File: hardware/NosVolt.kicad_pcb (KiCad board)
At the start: 2 copper layers, 100 x 60 mm, 122 parts, among them CN201 100nF, J101 INPUTS, J102 OUTPUTS, J201 BAT_SENSE, J202 BAT_NTC, J401 USB_C_Receptacle_USB2.0_16P, Q1101 2N7002, Q1102 AO4407A, Q801 2N7002, Q802 AO4407A, Q901 2N7002, Q902 AO4407A, SW101 SW_Reset, SW102 SSSS811101, U1001 INA226, U101 GMT028-05, U102 ESP32-S3-WROOM-1, U1201 INA226, U201 ADS1115IDGS, U301 MP2307DN-LF-Z, U401 AP7361-33ER-13, U402 USBLC6-2SC6, U501 INA226, U601 INA226, U701 INA226

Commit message: reanotate
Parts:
- moved NT902 7.47 mm to (191.4, 82.0), turned to 90 degrees
- moved NT904 7.44 mm to (185.5, 86.5), turned to 180 degrees
- moved NT901 2.17 mm to (187.6, 79.0), turned to 90 degrees
- moved NT903 2.17 mm to (186.2, 80.7), turned to -90 degrees
- renumbered C601 to C301, C602 to C302, C701 to C401, C702 to C402, C1101 to C501, C1201 to C502, C1102 to C503, C1202 to C504, C901 to C601, C1001 to C602, C902 to C603, C1002 to C604, C801 to C701, C501 to C702, C802 to C703, C502 to C704, C401 to C801, C402 to C802, C403 to C803, C404 to C804, C405 to C805, C301 to C901, C302 to C902, C303 to C903, C304 to C904, C305 to C905, C306 to C906, C307 to C907, D401 to D801, F401 to F801, J401 to J801, L301 to L901, NT601 to NT301, NT602 to NT302, NT701 to NT401, NT702 to NT402, NT1101 to NT501, NT1201 to NT502, NT1202 to NT503, NT901 to NT601, NT1001 to NT602, NT1002 to NT603, NT801 to NT701, NT501 to NT702, NT502 to NT703, NT303 to NT901, NT304 to NT902, NT301 to NT903, NT302 to NT904, Q1101 to Q501, Q1102 to Q502, Q901 to Q601, Q902 to Q602, Q801 to Q701, Q802 to Q702, R601 to R301, R602 to R302, R603 to R303, R701 to R401, R702 to R402, R703 to R403, R1101 to R501, R1102 to R502, R1103 to R503, R1201 to R504, R1104 to R505, R1202 to R506, R1203 to R507, R901 to R601, R902 to R602, R903 to R603, R1001 to R604, R904 to R605, R1002 to R606, R1003 to R607, R801 to R701, R802 to R702, R803 to R703, R501 to R704, R804 to R705, R502 to R706, R503 to R707, R401 to R801, R402 to R802, R301 to R901, R302 to R902, R303 to R903, R304 to R904, U601 to U301, U701 to U401, U1201 to U501, U1001 to U601, U501 to U701, U401 to U801, U402 to U802, U301 to U901
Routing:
- net Net-(NT901-Pad2): track 0.00 -> 12.5 mm, vias 0 -> 2
- net /MP2307/SW: track 18.1 -> 5.59 mm, vias 2 -> 0
- net GND: track 74.4 -> 70.9 mm
- net Net-(NT904-Pad1): track 0.00 -> 3.56 mm

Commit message: text
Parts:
- moved C901 2.58 mm to (179.3, 76.8)
- moved C902 1.73 mm to (184.3, 76.8)
- moved NT901 0.72 mm to (188.0, 78.4), turned to 45 degrees
- moved R403 0.50 mm to (136.7, 57.8)
- moved L901 0.41 mm to (183.8, 84.0)
- moved NT904 0.38 mm to (185.1, 86.7)
- moved R904 0.31 mm to (189.6, 86.2)
- moved U101 0.28 mm to (152.7, 63.0)
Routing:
- net Net-(U901-BS): track 10.6 -> 8.28 mm
- net Net-(NT901-Pad2): track 12.5 -> 11.8 mm
- net Net-(NT904-Pad1): track 3.56 -> 4.15 mm
- net +3V3: vias 19 -> 18

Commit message: Add logo
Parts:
- added G***: LOGO, LOGO, F.Cu at (146.9, 82.6)
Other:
- board text added: "Version 1.0"

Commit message: page numbers
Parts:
- U901: footprint Package_SO:SOIC-8-1EP_3.9x4.9mm_P1.27mm_EP2.29x3mm_ThermalVias -> NosLib:SOIC-8-1EP_3.9x4.9mm_P1.27mm_EP2.29x3mm_ThermalVias
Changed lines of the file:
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@@
 		(embedded_fonts no)
 	)
-	(footprint "Package_SO:SOIC-8-1EP_3.9x4.9mm_P1.27mm_EP2.29x3mm_ThermalVias"
+	(footprint "NosLib:SOIC-8-1EP_3.9x4.9mm_P1.27mm_EP2.29x3mm_ThermalVias"
 		(layer "F.Cu")
 		(at 192.28 80.55)
@@
 			(pinfunction "GND")
 			(pintype "power_in")
-			(zone_connect 2)
 		)
 		(pad "5" smd roundrect
@@
 			(at -0.65 -1)
 			(size 0.5 0.5)
-			(drill 0.2)
+			(drill 0.3)
+			(property pad_prop_heatsink)
+			(layers "*.Cu" "B.Paste")
+			(remove_unused_layers no)
+			(net 69 "/MP2307/PWR_GND")
+			(pinfunction "EP")
+			(pintype "input")
+		)
+		(pad "9" thru_hole circle
+			(at -0.65 0)
+			(size 0.5 0.5)
+			(drill 0.3)
 			(property pad_prop_heatsink)
 			(layers "*.Cu")
@@
 		)
 		(pad "9" thru_hole circle
-			(at -0.65 0)
-			(size 0.5 0.5)
-			(drill 0.2)
-			(property pad_prop_heatsink)
-			(layers "*.Cu")
-			(remove_unused_layers no)
-			(net 69 "/MP2307/PWR_GND")
-			(pinfunction "EP")
-			(pintype "input")
-		)
-		(pad "9" thru_hole circle
 			(at -0.65 1)
 			(size 0.5 0.5)
-			(drill 0.2)
+			(drill 0.3)
 			(property pad_prop_heatsink)
 			(layers "*.Cu")
@@
 			(at 0.65 -1)
 			(size 0.5 0.5)
-			(drill 0.2)
+			(drill 0.3)
 			(property pad_prop_heatsink)
 			(layers "*.Cu")
@@
 			(at 0.65 0)
 			(size 0.5 0.5)
-			(drill 0.2)
+			(drill 0.3)
 			(property pad_prop_heatsink)
 			(layers "*.Cu")
@@
 			(at 0.65 1)
 			(size 0.5 0.5)
-			(drill 0.2)
+			(drill 0.3)
 			(property pad_prop_heatsink)
 			(layers "*.Cu")

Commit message: Test points
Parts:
- removed J202: BAT_NTC, Connector_JST:JST_GH_SM02B-GHS-TB_1x02-1MP_P1.25mm_Horizontal
- removed R201: 1K, Resistor_SMD:R_0603_1608Metric_Pad0.98x0.95mm_HandSolder
- added C104: 100nF, Capacitor_SMD:C_0603_1608Metric, F.Cu at (115.9, 52.6)
- added J103: BAT_NTC, Connector_JST:JST_GH_SM03B-GHS-TB_1x03-1MP_P1.25mm_Horizontal, F.Cu at (125.2, 41.2)
- added R105: 4.7K, Resistor_SMD:R_0603_1608Metric_Pad0.98x0.95mm_HandSolder, F.Cu at (114.7, 77.6)
- added TP_101: BOOT, NosLib:TestPoint_Pad_1.0x1.0mm, F.Cu at (104.2, 84.0)
- added TP_102: +5V_USB, NosLib:TestPoint_Pad_1.0x1.0mm, F.Cu at (161.8, 81.0)
- added TP_103: SDA, NosLib:TestPoint_Pad_1.0x1.0mm, F.Cu at (112.0, 91.3)
- added TP_104: SCL, NosLib:TestPoint_Pad_1.0x1.0mm, F.Cu at (112.0, 93.7)
- added TP_105: GND, NosLib:TestPoint_Pad_1.0x1.0mm, F.Cu at (112.0, 96.2)
- added TP_106: MTCK, NosLib:TestPoint_Pad_1.0x1.0mm, F.Cu at (112.0, 81.6)
- added TP_107: MTDO, NosLib:TestPoint_Pad_1.0x1.0mm, F.Cu at (112.0, 84.0)
- added TP_108: MTDI, NosLib:TestPoint_Pad_1.0x1.0mm, F.Cu at (112.0, 86.5)
- added TP_109: MTMS, NosLib:TestPoint_Pad_1.0x1.0mm, F.Cu at (112.0, 88.9)
- added TP_110: DALLAS, NosLib:TestPoint_Pad_1.0x1.0mm, F.Cu at (104.2, 81.6)
- added TP_112: TX, NosLib:TestPoint_Pad_1.0x1.0mm, F.Cu at (104.2, 88.9)
- added TP_113: RX, NosLib:TestPoint_Pad_1.0x1.0mm, F.Cu at (104.2, 86.5)
- added TP_115: +3V3_USB, NosLib:TestPoint_Pad_1.0x1.0mm, F.Cu at (161.8, 83.4)
- added TP_116: GND, NosLib:TestPoint_Pad_1.0x1.0mm, F.Cu at (188.3, 95.2)
- added TP_117: +3V3_UPS, NosLib:TestPoint_Pad_1.0x1.0mm, F.Cu at (175.1, 84.4)
- added TP_118: +12V_UPS, NosLib:TestPoint_Pad_1.0x1.0mm, F.Cu at (175.1, 82.0)
- added TP_123: +3V3, NosLib:TestPoint_Pad_1.0x1.0mm, F.Cu at (181.6, 95.2)
- added U102: DS18B20Z, Package_SO:SOIC-8_3.9x4.9mm_P1.27mm, F.Cu at (106.9, 72.7)
- moved NT901 2.98 mm to (185.1, 77.8), turned to 0 degrees
- moved NT903 2.39 mm to (183.9, 80.5)
- moved R101 0.70 mm to (114.7, 74.6), turned to 180 degrees
- moved H104 0.36 mm to (198.7, 93.8)
- moved H101 0.12 mm to (106.7, 41.8)
- moved H103 0.07 mm to (106.7, 93.8)
- renumbered U102 to U103
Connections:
- net /+12V_UPS renamed +12V_UPS
- net /SHUNT_OUT_LO1 renamed /SHUNT_USP_LO1
- net /SHUNT_OUT_LO2 renamed /SHUNT_LO_OUT2
- net /SHUNT_OUT_LO3 renamed /SHUNT_USP_LO3
- CN201 pad 1: Net-(U201-AIN3) -> unconnected-(CN201-C1.1-Pad1)
- J101 pad 1: /SHUNT_OUT_LO -> /SHUNT_OUT_HI
- J101 pad 2: /SHUNT_OUT_HI -> /SHUNT_GND
- J102 pad 2: /SHUNT_OUT_HI -> /SHUNT_GND
- J102 pad 4: /SHUNT_OUT_HI -> /SHUNT_GND
- J102 pad 6: /SHUNT_OUT_HI -> /SHUNT_GND
- NT101 pad 2: /SHUNT_OUT_LO -> /SHUNT_OUT_HI
- NT501 pad 2: /SHUNT_OUT_LO -> /SHUNT_OUT_HI
- NT601 pad 2: /SHUNT_OUT_LO -> /SHUNT_OUT_HI
- NT701 pad 2: /SHUNT_OUT_LO -> /SHUNT_OUT_HI
- Q502 pad 1: /SHUNT_OUT_LO -> /SHUNT_OUT_HI
- Q502 pad 2: /SHUNT_OUT_LO -> /SHUNT_OUT_HI
- Q502 pad 3: /SHUNT_OUT_LO -> /SHUNT_OUT_HI
- Q602 pad 1: /SHUNT_OUT_LO -> /SHUNT_OUT_HI
- Q602 pad 2: /SHUNT_OUT_LO -> /SHUNT_OUT_HI
- Q602 pad 3: /SHUNT_OUT_LO -> /SHUNT_OUT_HI
- Q702 pad 1: /SHUNT_OUT_LO -> /SHUNT_OUT_HI
- Q702 pad 2: /SHUNT_OUT_LO -> /SHUNT_OUT_HI
- Q702 pad 3: /SHUNT_OUT_LO -> /SHUNT_OUT_HI
- RN202 pad 4: Net-(J202-Pin_2) -> unconnected-(RN202-R4.1-Pad4)
- RN202 pad 5: GND -> unconnected-(RN202-R4.2-Pad5)
- U103 pad 31: unconnected-(U102-GPIO38/FSPIWP/SUBSPIWP-Pad31) -> DALLAS
- U103 pad 32: unconnected-(U102-MTCK/GPIO39/CLK_OUT3/SUBSPICS1-Pad32) -> Net-(U103-MTCK/GPIO39/CLK_OUT3/SUBSPICS1)
- U103 pad 33: unconnected-(U102-MTDO/GPIO40/CLK_OUT2-Pad33) -> Net-(U103-MTDO/GPIO40/CLK_OUT2)
- U103 pad 34: unconnected-(U102-MTDI/GPIO41/CLK_OUT1-Pad34) -> Net-(U103-MTDI/GPIO41/CLK_OUT1)
- U103 pad 35: unconnected-(U102-MTMS/GPIO42-Pad35) -> Net-(U103-MTMS/GPIO42)
- U103 pad 36: unconnected-(U102-U0RXD/GPIO44/CLK_OUT2-Pad36) -> Net-(U103-U0RXD/GPIO44/CLK_OUT2)
- U103 pad 37: unconnected-(U102-U0TXD/GPIO43/CLK_OUT1-Pad37) -> Net-(U103-U0TXD/GPIO43/CLK_OUT1)
- U201 pad 7: Net-(U201-AIN3) -> unconnected-(U201-AIN3-Pad7)
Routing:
- net /SHUNT_OUT_LO: track 82.3 -> 0.00 mm, vias 3 -> 0
- net DALLAS: track 0.00 -> 63.1 mm, vias 0 -> 2
- net /SHUNT_GND: track 0.00 -> 43.4 mm
- net /SHUNT_OUT_HI: track 43.4 -> 82.3 mm, vias 0 -> 3
- net +3V3: track 309.1 -> 338.0 mm
- net Net-(J202-Pin_2): track 26.5 -> 0.00 mm
- net SDA: track 151.0 -> 173.8 mm, vias 8 -> 9
- net SCL: track 151.3 -> 170.7 mm, vias 7 -> 8
- net BOOT: track 3.99 -> 21.5 mm, vias 0 -> 2
- net Net-(U103-U0TXD/GPIO43/CLK_OUT1): track 0.00 -> 15.0 mm, vias 0 -> 2
- net Net-(U201-AIN3): track 14.4 -> 0.00 mm, vias 2 -> 0
- net Net-(U103-U0RXD/GPIO44/CLK_OUT2): track 0.00 -> 14.4 mm, vias 0 -> 2
- net +3V3_USB: track 17.6 -> 27.8 mm
- net Net-(U103-MTMS/GPIO42): track 0.00 -> 8.88 mm
- net Net-(U103-MTDI/GPIO41/CLK_OUT1): track 0.00 -> 7.98 mm
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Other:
- outline, holes or cut-outs redrawn
- board text added: "+3V3"
- board text added: "DALLAS"
- board text added: "UPS 12V"
- board text added: "UPS 3V3"
- board text added: "USB 3V3"
- board text added: "USB 5V"
- board text removed: "NTC1"
- board text removed: "NTC2"

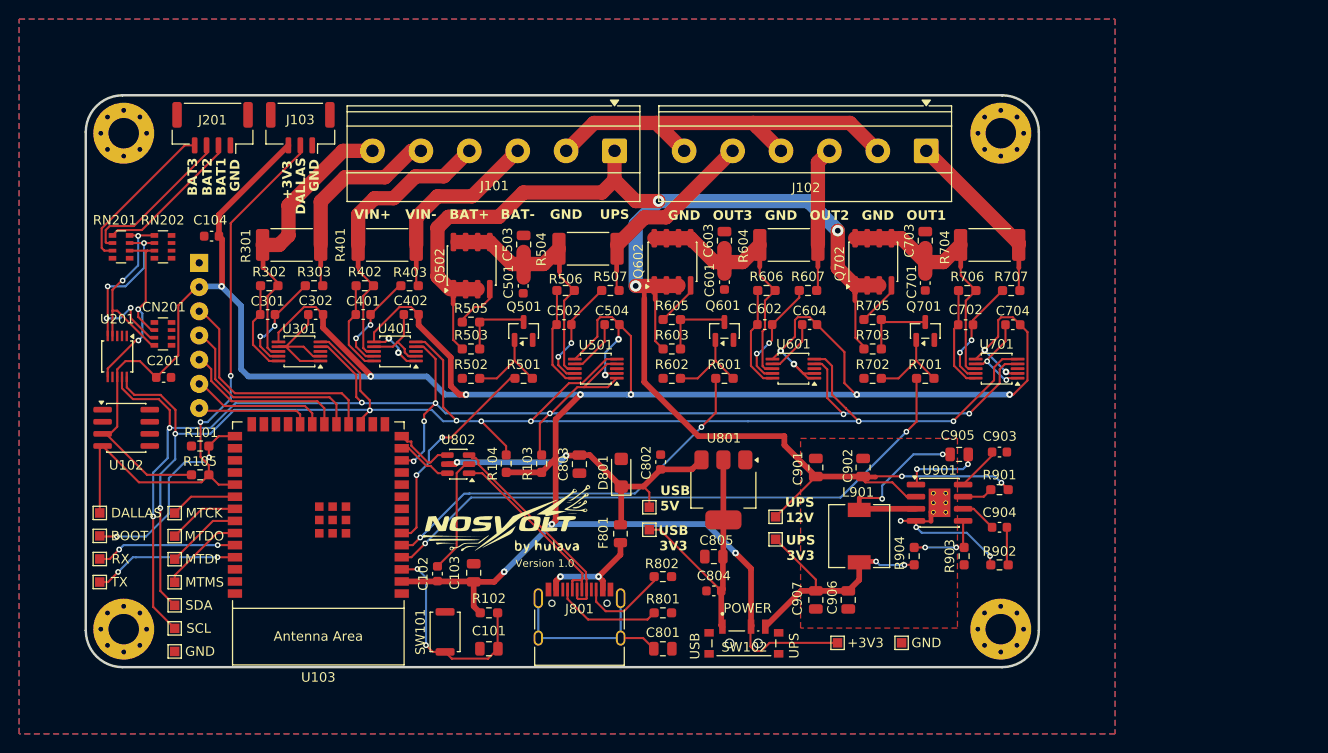
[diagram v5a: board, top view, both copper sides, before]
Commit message: hand soldering footprints and led
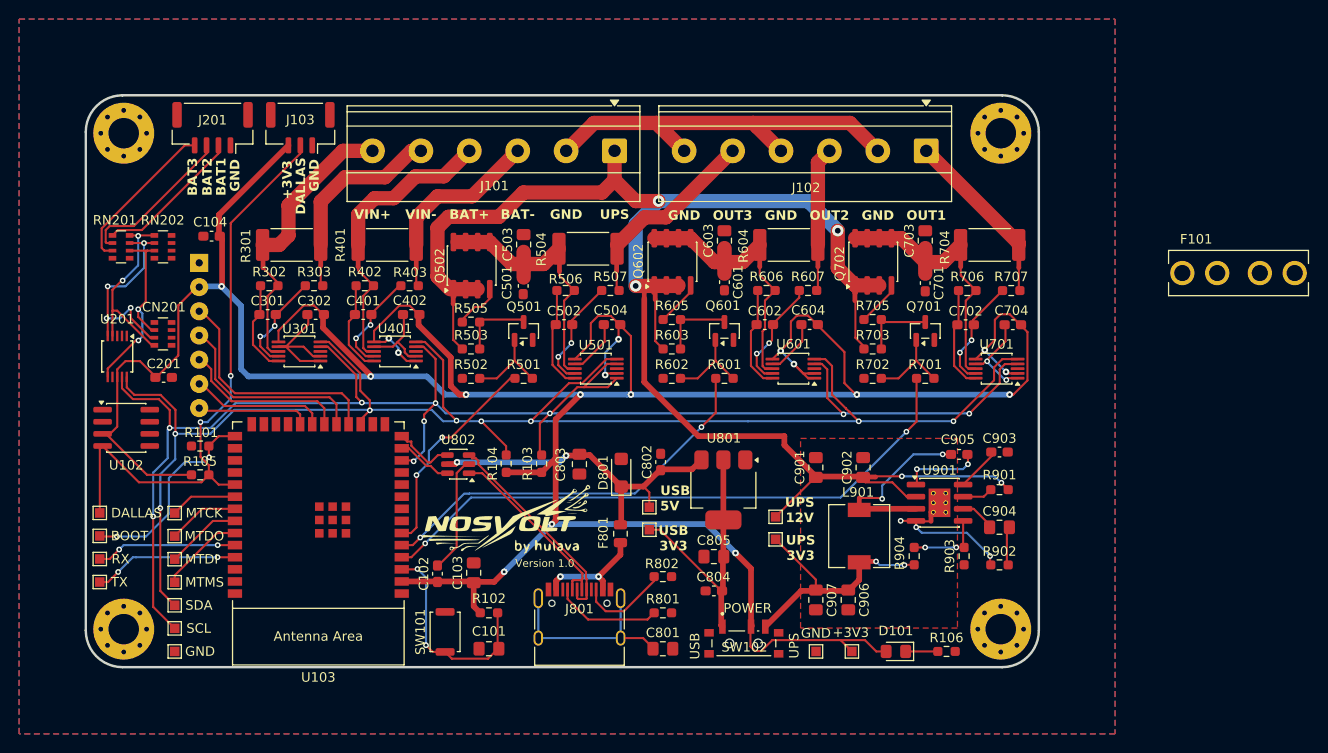
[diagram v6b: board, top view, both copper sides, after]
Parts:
- added D101: LED, LED_SMD:LED_0805_2012Metric_Pad1.15x1.40mm_HandSolder, F.Cu at (187.7, 96.2)
- added F101: Fuse, NosLib:FUSE_3544-2, F.Cu at (223.7, 56.5)
- added R106: 1K, Resistor_SMD:R_0603_1608Metric_Pad0.98x0.95mm_HandSolder, F.Cu at (193.0, 96.2)
- C101, C103, C503, C603, C703, C801, C803, C805, C901, C902, C906, C907: footprint Capacitor_SMD:C_0805_2012Metric -> Capacitor_SMD:C_0805_2012Metric_Pad1.18x1.45mm_HandSolder
- C102, C104, C201, C301, C302, C401, C402, C501, C502, C504, C601, C602, C604, C701, C702, C704, C802, C804, C903: footprint Capacitor_SMD:C_0603_1608Metric -> Capacitor_SMD:C_0603_1608Metric_Pad1.08x0.95mm_HandSolder
- C904: footprint Capacitor_SMD:C_0603_1608Metric -> Capacitor_SMD:C_0805_2012Metric_Pad1.18x1.45mm_HandSolder
- C905: footprint Capacitor_SMD:C_0805_2012Metric -> Capacitor_SMD:C_0603_1608Metric_Pad1.08x0.95mm_HandSolder
- moved TP_116 9.02 mm to (179.3, 96.2)
- moved TP_123 1.75 mm to (183.1, 96.2)
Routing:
- net +3V3: track 338.0 -> 346.9 mm
- net Net-(D101-K): track 0.00 -> 3.37 mm

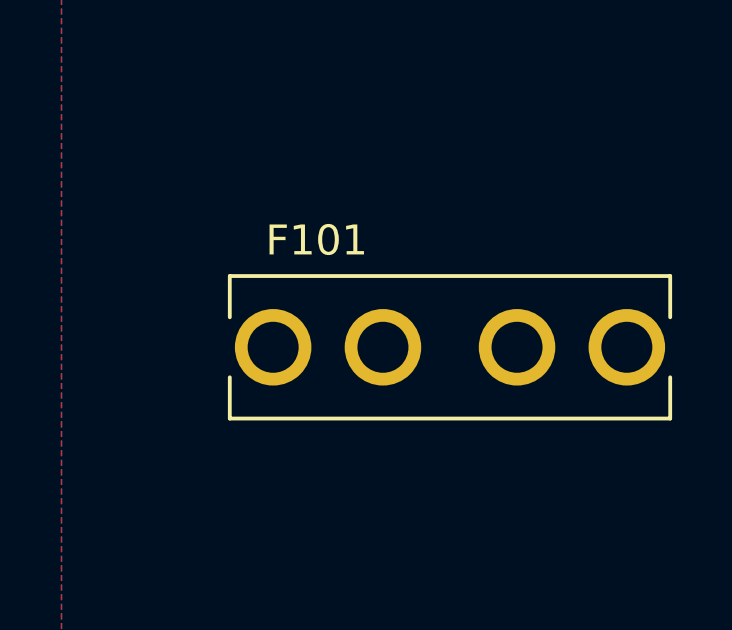
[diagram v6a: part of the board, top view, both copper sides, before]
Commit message: remove fuse
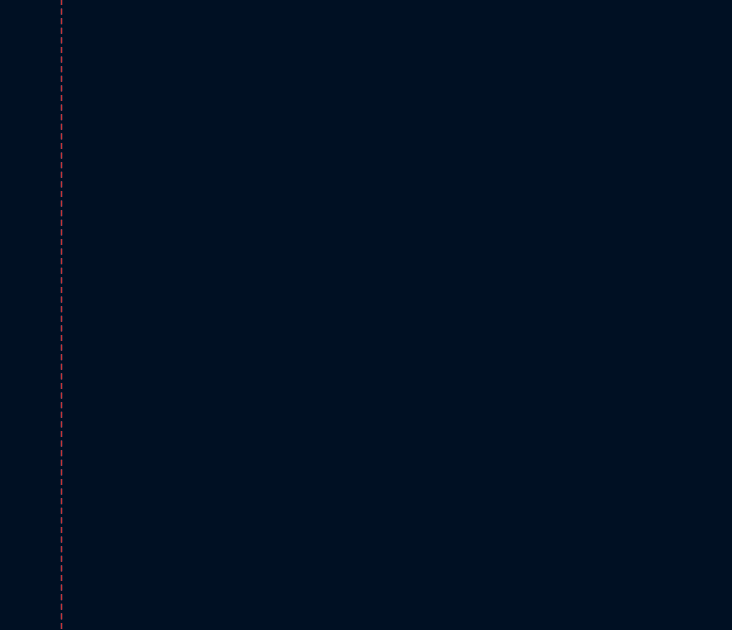
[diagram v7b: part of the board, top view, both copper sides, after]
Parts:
- removed F101: Fuse, NosLib:FUSE_3544-2

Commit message: PWR_FLG
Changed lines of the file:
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@@
 		(tags "capacitor handsolder")
 		(property "Reference" "C701"
-			(at 0 -1.43 270)
+			(at -0.2 1.5818 270)
 			(layer "F.SilkS")
 			(effects
@@
 		(tags "capacitor handsolder")
 		(property "Reference" "C601"
-			(at 0 -1.43 270)
+			(at -0.3 1.7112 270)
 			(layer "F.SilkS")
 			(effects
@@
 		(min_thickness 0.25)
 		(filled_areas_thickness no)
-		(fill yes
+		(fill
 			(thermal_gap 0.5)
 			(thermal_bridge_width 0.5)
@@
 		(min_thickness 0.2)
 		(filled_areas_thickness no)
-		(fill yes
+		(fill
 			(thermal_gap 0.5)
 			(thermal_bridge_width 0.5)
